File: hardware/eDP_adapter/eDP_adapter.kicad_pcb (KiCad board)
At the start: 2 copper layers, 36.3 x 28.4 mm, 89 parts, among them J1 DF12NB(3.0)-30DS-0.5V(51), J2 DF12NB(3.0)-30DS-0.5V(51), J3 Conn_01x40, J4 Barrel_Jack_MountingPin, Q1 2N7002WT1G, U1 NCS8801, U2 EA3036A, U3 MT3608

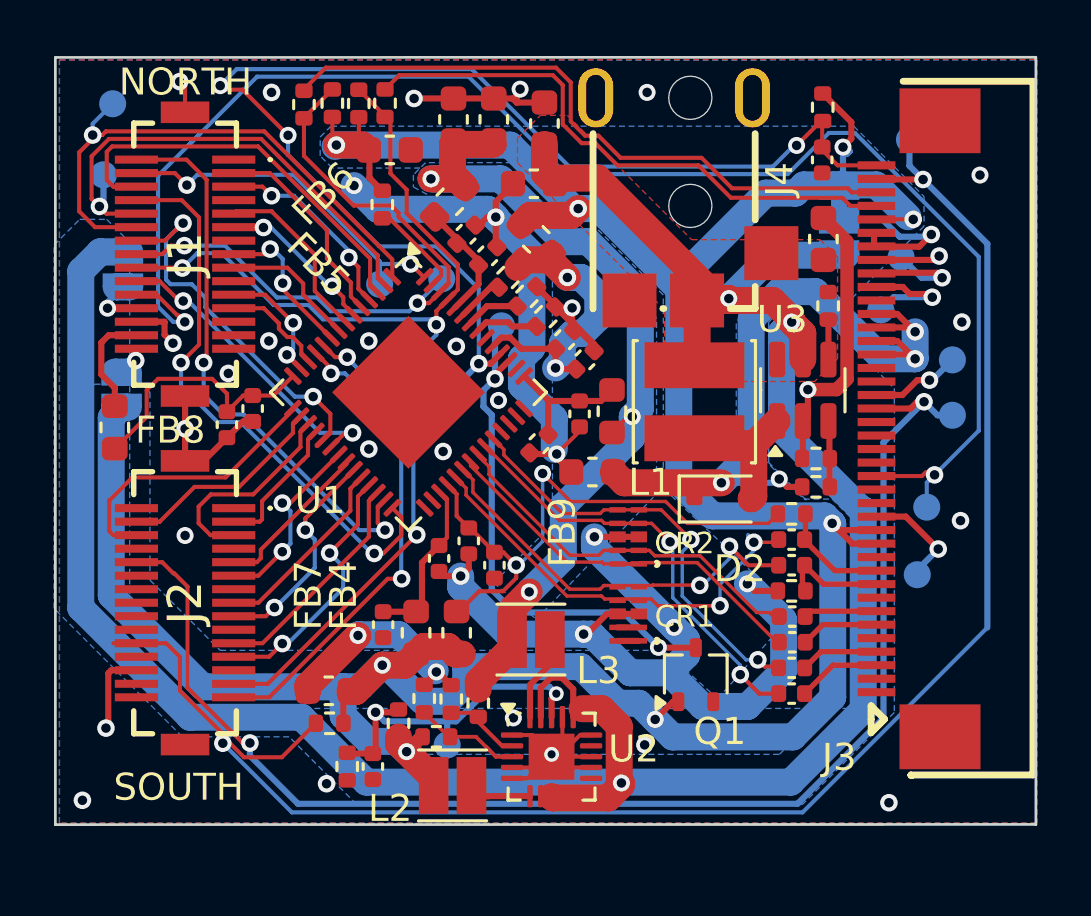
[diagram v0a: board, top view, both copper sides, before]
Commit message: make eDP adaoter 4 layer and misc fixes (like missing crystal)
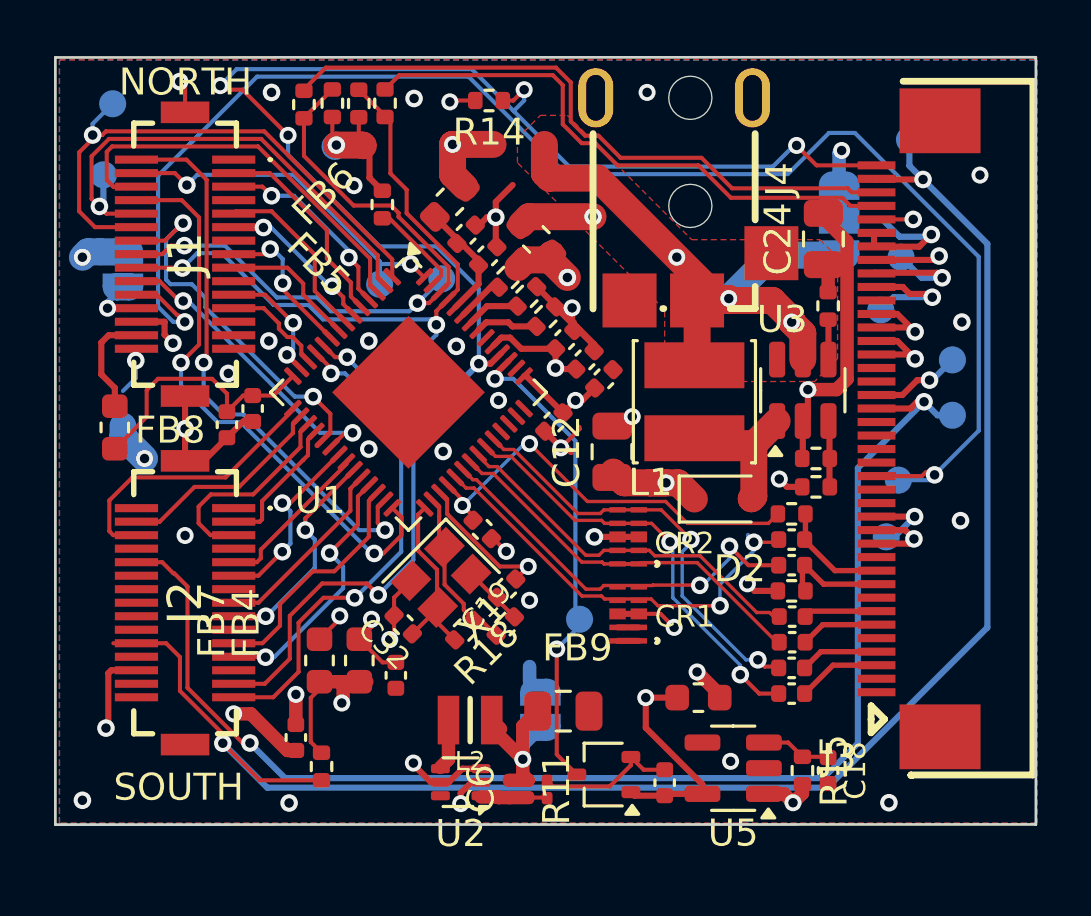
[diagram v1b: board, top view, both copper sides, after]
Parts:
- removed C28: 0.1uF, Capacitor_SMD:C_0402_1005Metric
- removed C29: 10u, Capacitor_SMD:C_0603_1608Metric
- removed C30: 0.1uF, Library:C_0402_1005Metric
- removed C31: 0.1u, Capacitor_SMD:C_0603_1608Metric
- removed L3: 1.5uH, Inductor_SMD:L_Cenker_CKCS201610
- removed R16, R17, R22: 100k, Resistor_SMD:R_0402_1005Metric
- removed TP10, TP11: TestPoint_Small, TestPoint:TestPoint_Pad_D1.0mm
- added C19: 18pF, Library:C_0402_1005Metric, F.Cu at (120.2, 133.9)
- added C32: 18pF, Library:C_0402_1005Metric, F.Cu at (116.5, 133.9)
- added R18: 1M, Resistor_SMD:R_0402_1005Metric, F.Cu at (118.7, 134.1)
- added TP8: TestPoint_Small, TestPoint:TestPoint_Pad_D1.0mm, B.Cu at (123.0, 133.7)
- added U5: TPNCP115ASN120T2G, Package_TO_SOT_SMD:SOT-23-5, F.Cu at (128.7, 139.2)
- added X1: 24MHz, CL=18PF, Library:Crystal_SMD_2520-4Pin_2.5x2.0mm, F.Cu at (117.9, 132.2)
- C12, C2: value 0.1u -> 10uF 25V; footprint Capacitor_SMD:C_0603_1608Metric -> Capacitor_SMD:C_0805_2012Metric
- C18: value 0.1u -> 0.1uF; footprint Capacitor_SMD:C_0603_1608Metric -> Library:C_0402_1005Metric
- C24: value 10u -> 10uF 25V; footprint Capacitor_SMD:C_0603_1608Metric -> Capacitor_SMD:C_0805_2012Metric
- C25: value 10u -> 2.2uF; footprint Capacitor_SMD:C_0603_1608Metric -> Library:C_0402_1005Metric
- C6: value 10u -> 100pF; footprint Capacitor_SMD:C_0603_1608Metric -> Capacitor_SMD:C_0201_0603Metric
- L2: value 1.5uH -> 2.2uH; footprint Inductor_SMD:L_Cenker_CKCS201610 -> Library:Murata_DFE201612P-2R2M=P2
- Q1: value 2N7002WT1G -> NX3008NBKW,115
- R11: value 150k 1% -> 15k; footprint Resistor_SMD:R_0402_1005Metric -> Resistor_SMD:R_0201_0603Metric
- R12: value 150k 1% -> 4.7k; footprint Resistor_SMD:R_0402_1005Metric -> Resistor_SMD:R_0201_0603Metric
- R14: value 680k 1% -> 100k
- R15: value 150k 1% -> 10k
- U2: value EA3036A -> TLV62569APDRL; footprint Package_DFN_QFN:WQFN-20-1EP_3x3mm_P0.4mm_EP1.7x1.7mm -> Package_TO_SOT_SMD:SOT-563
- moved C18 27.1 mm to (132.2, 139.3)
- moved R14 23.6 mm to (119.7, 114.5)
- moved C2 21.7 mm to (122.4, 137.1), turned to 0 degrees
- moved JP2 19.5 mm to (121.5, 137.1), turned to -90 degrees
- moved C12 13.6 mm to (124.2, 127.5), turned to 90 degrees
- moved R15 12.3 mm to (131.2, 139.3)
- moved C25 11.8 mm to (126.2, 139.8), turned to 90 degrees
- moved FB9 11.1 mm to (127.4, 136.6), turned to 0 degrees
- moved C6 7.60 mm to (120.4, 140.0), turned to 90 degrees
- moved C11 5.47 mm to (116.2, 135.8)
- moved C8 5.28 mm to (112.5, 138.1)
- moved R11 5.10 mm to (121.1, 140.0), turned to -90 degrees
- moved Q1 5.02 mm to (123.9, 139.4), turned to 180 degrees
- moved R12 4.88 mm to (121.8, 140.0)
- moved FB4 3.74 mm to (114.8, 135.2)
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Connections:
- C12 pad 1: GND -> /BACKLIGHT_POWER
- C12 pad 2: +1V2 -> GND
- C18 pad 1: GND -> Net-(U5-EN)
- C18 pad 2: +1V2 -> GND
- C2 pad 1: GND -> /+3V3_DISP
- C2 pad 2: +3V3 -> GND
- C24 pad 1: GND -> +5V
- C24 pad 2: +5V -> GND
- C25 pad 1: GND -> +1V2
- C25 pad 2: /BACKLIGHT_POWER -> GND
- C6 pad 1: GND -> Net-(U2-FB)
- C6 pad 2: +3V3 -> /+3V3_DISP
- J1 pad 30: +3V3_MCU -> +3V3
- J3 pad 12: +3V3 -> /+3V3_DISP
- J3 pad 13: +3V3 -> /+3V3_DISP
- JP2 pad 2: +3V3_MCU -> /+3V3_DISP
- L2 pad 1: +3V3 -> /+3V3_DISP
- L2 pad 2: Net-(U2-SW2) -> Net-(U2-SW)
- Q1 pad 1: +3V3 -> +1V2
- R11 pad 1: Net-(U2-FB2) -> /+3V3_DISP
- R11 pad 2: GND -> Net-(U2-FB)
- R12 pad 2: Net-(U2-FB3) -> Net-(U2-FB)
- R14 pad 1: Net-(U2-FB2) -> RSTB
- R15 pad 1: +1V2 -> Net-(U5-EN)
- R15 pad 2: Net-(U2-FB3) -> +3V3
- U1 pad 29: unconnected-(U1-XTALIN-Pad29) -> /XTALI
- U1 pad 30: unconnected-(U1-XTALOUT-Pad30) -> /XTALO
- U2 pad 1: GND -> Net-(U2-FB)
- U2 pad 2: Net-(U2-FB3) -> GND
- U2 pad 3: Net-(U2-FB2) -> +5V
- U2 pad 4: GND -> Net-(U2-SW)
- U2 pad 5: GND -> +5V
- U2 pad 6: Net-(U2-SW2) -> unconnected-(U2-NC-Pad6)
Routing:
- net GND: track 111.0 -> 56.9 mm, vias 38 -> 36
- net /+3V3_DISP: track 0.00 -> 28.7 mm, vias 0 -> 2
- net /BACKLIGHT_POWER: track 29.1 -> 11.9 mm
- net AVDD_1V2: track 5.48 -> 22.4 mm, vias 0 -> 2
- net XVDD_3V3: track 7.12 -> 20.2 mm, vias 0 -> 3
- net Net-(U2-EN3): track 12.7 -> 0.00 mm, vias 2 -> 0
- net /XTALI: track 0.00 -> 6.87 mm
- net /XTALO: track 0.00 -> 6.13 mm
- net +1V2: track 32.3 -> 36.7 mm
- net Net-(U2-FB2): track 4.11 -> 0.00 mm
- net AVDD_3V3: track 20.9 -> 24.2 mm, vias 2 -> 3
- net +3V3: track 116.6 -> 113.4 mm, vias 8 -> 9
- net Net-(U2-SW3): track 3.16 -> 0.00 mm
- net Net-(U2-FB3): track 2.87 -> 0.00 mm
- net Net-(U5-EN): track 0.00 -> 2.61 mm
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- added copper zone on In2.Cu, net +1V2
- added copper zone on In2.Cu, net +3V3
- added copper zone on In2.Cu, net +5V
- added copper zone on In1.Cu, net /BACKLIGHT_POWER
- added copper zone on In2.Cu, net AVDD_3V3
- added copper zone on In2.Cu, net DVDD_3V3
- added copper zone on In1.Cu, net GND
- removed copper zone on B.Cu, net +1V2
- removed copper zone on B.Cu, net +3V3
- removed copper zone on B.Cu, net +5V
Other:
- copper layers 2 -> 4

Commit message: fixed mixup of pins G5/G4 (3rd diff pair ODD) and DE/PCLK (3rd diff pair EVEN), now with correct polarity for diff pairs
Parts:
- added C26: 0.1uF, Library:C_0402_1005Metric, F.Cu at (132.3, 115.0)
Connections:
- J2 pad 4: G4 -> G5
- J2 pad 6: G5 -> G4
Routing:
- net G5: track 10.4 -> 7.99 mm
- net RSTB: track 47.1 -> 48.5 mm
- net G4: track 7.89 -> 8.42 mm

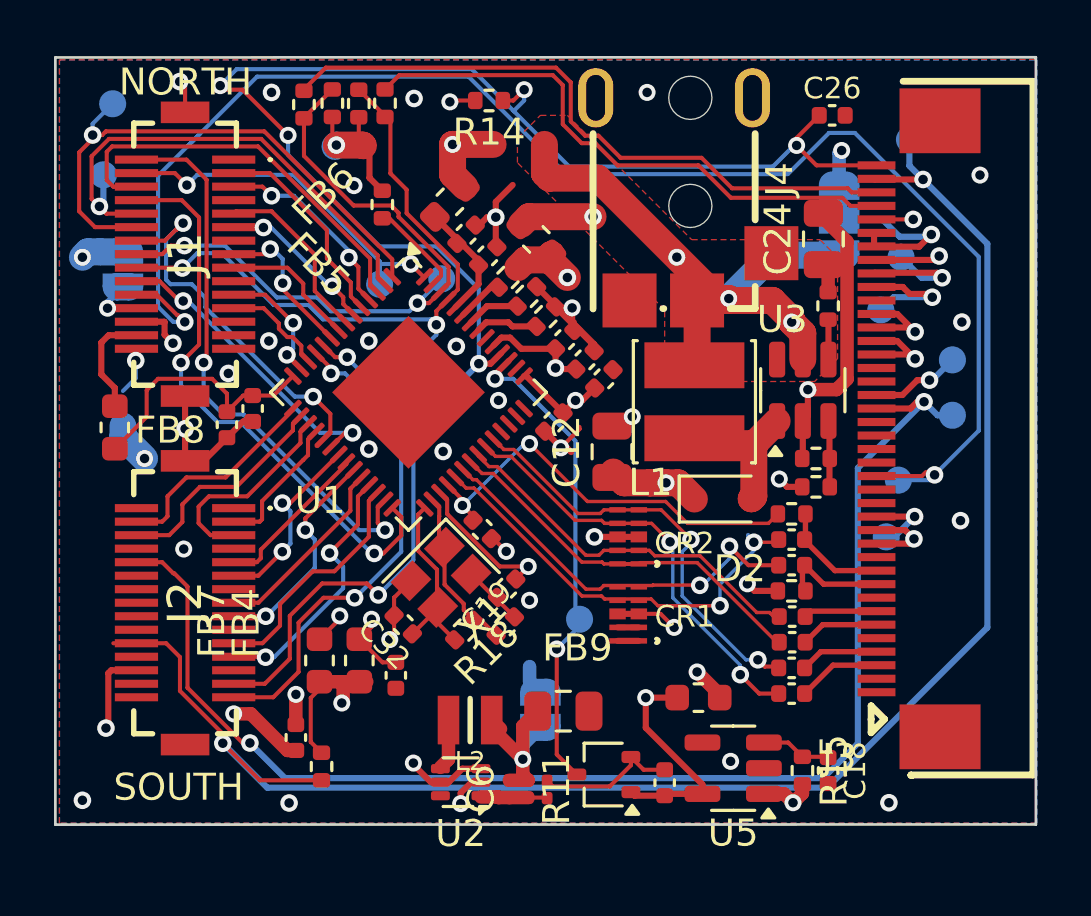
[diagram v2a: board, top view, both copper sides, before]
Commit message: Add I2C connector for touch and replace 40pin touch with 30pin. Separate schematics in sheets. Impedance control on diff pairs
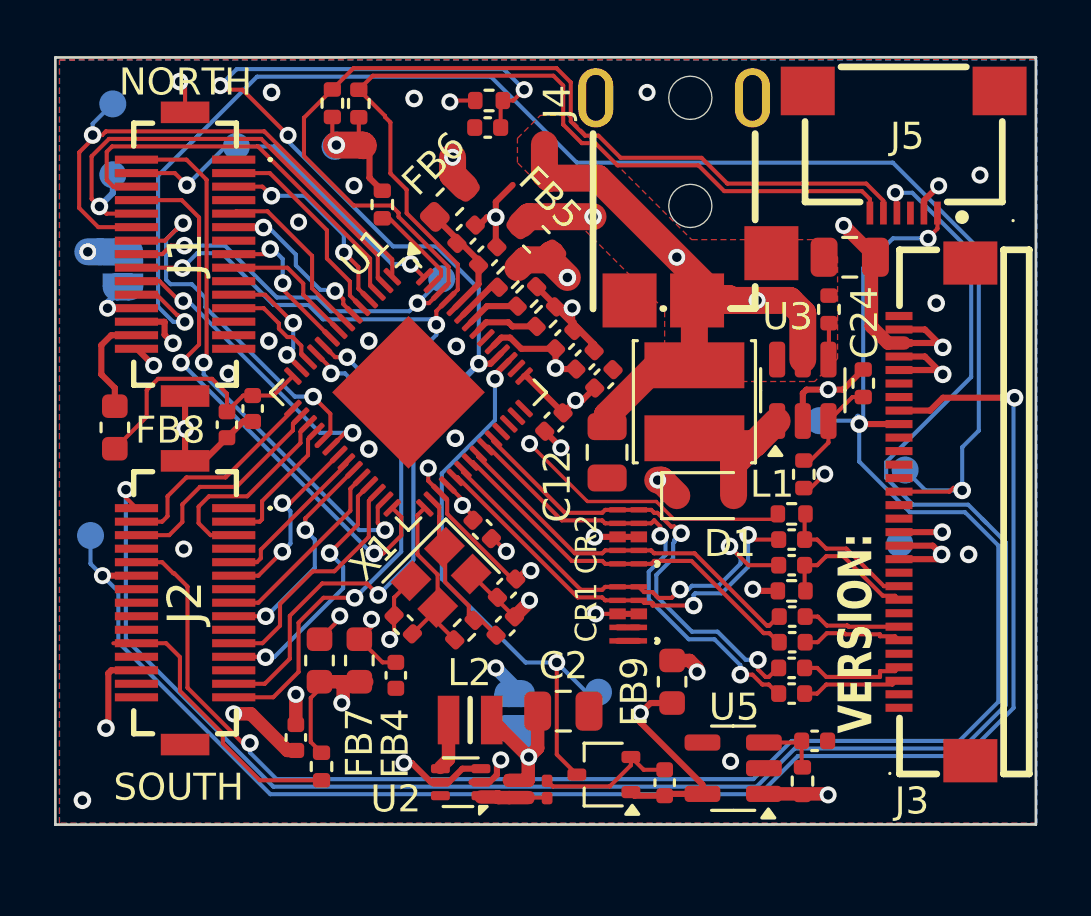
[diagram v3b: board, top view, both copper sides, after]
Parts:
- removed D2: 1N5819WS, Diode_SMD:D_SOD-323
- removed JP3: SolderJumper_3_Bridged12, Jumper:SolderJumper-3_P1.3mm_Bridged12_RoundedPad1.0x1.5mm
- removed R10, R13: 0, Resistor_SMD:R_0402_1005Metric
- removed R20: 150K 1%, Resistor_SMD:R_0402_1005Metric
- removed R21: 8.06K 1%, Resistor_SMD:R_0402_1005Metric
- removed TP1, TP15, TP16, TP2, TP3: TestPoint_Small, TestPoint:TestPoint_Pad_D1.0mm
- added D1: 1N5819WS, Diode_SMD:D_SOD-323, F.Cu at (127.7, 129.1)
- added J5: Conn_01x06_Socket, easyeda2kicad:FPC-SMD_FH52K-6S-0.5SH, F.Cu at (135.0, 116.4)
- added R16: 10k, Resistor_SMD:R_0402_1005Metric, F.Cu at (132.2, 122.2)
- added R17: 8.06K 1%, Resistor_SMD:R_0402_1005Metric, F.Cu at (133.5, 125.0)
- added TP10: TestPoint_Small, TestPoint:TestPoint_Pad_D1.0mm, B.Cu at (110.3, 116.2)
- added TP11: TestPoint_Small, TestPoint:TestPoint_Pad_D1.0mm, B.Cu at (105.7, 117.2)
- J3: value Conn_01x40 -> Conn_01x30; footprint Library:FPC-SMD_40P-P0.50_L4.4-W25.6 -> easyeda2kicad:FPC-SMD_30P-P0.50_FPC-0.5FX-30PWBH15
- R19: value 10k -> 150K 1%
- moved G*** 33.3 mm to (136.4, 114.6)
- moved TP4 32.6 mm to (104.9, 130.6)
- moved TP12 13.8 mm to (105.7, 114.6)
- moved TP14 13.4 mm to (117.1, 123.8)
- moved C26 12.8 mm to (119.6, 115.5), turned to 180 degrees
- moved R19 6.30 mm to (131.3, 128.3), turned to -90 degrees
- moved TP5 4.93 mm to (131.9, 126.3)
- moved G*** 4.25 mm to (127.3, 132.5)
- moved J3 3.23 mm to (136.1, 129.7)
- moved TP8 2.79 mm to (123.7, 136.4)
- moved TP13 2.76 mm to (117.9, 121.1)
- moved C18 1.21 mm to (131.7, 138.2), turned to 0 degrees
- moved C24 1.19 mm to (133.0, 120.3), turned to 180 degrees
- moved FB9 1.14 mm to (126.4, 136.0), turned to 90 degrees
- moved JP2 0.95 mm to (120.6, 137.1)
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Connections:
- net +5V_MCU renamed Net-(J1-23)
- net /+3V3_DISP renamed +3V3_DISP
- net /AUX0_N renamed AUX0_N
- net /AUX0_P renamed AUX0_P
- net /LCD_TEST renamed /IO/LCD_TEST
- net /SCK2 renamed /IO/SCK2
- net /SDA2 renamed /IO/SDA2
- net /TX0_N renamed TX0_N
- net /TX0_P renamed TX0_P
- net /TX1_N renamed TX1_N
- net /TX1_P renamed TX1_P
- net Net-(U1-DPAUX_N) renamed /DPAUX_N
- net Net-(U1-DPAUX_P) renamed /DPAUX_P
- net Net-(U1-DPO0_N) renamed /DPO0_N
- net Net-(U1-DPO0_P) renamed /DPO0_P
- net Net-(U1-DPO1_N) renamed /DPO1_N
- net Net-(U1-DPO1_P) renamed /DPO1_P
- C12 pad 1: /BACKLIGHT_POWER -> +5V
- C24 pad 1: +5V -> BACKLIGHT_POWER
- C32 pad 1: /XTALI -> GND
- C32 pad 2: GND -> /XTALI
- J2 pad 12: /TP_PWM -> /IO/LCD_PWM
- J2 pad 2: unconnected-(J2-1-Pad2) -> /IO/TP_INT
- J3 pad 23: /LCD_PWM -> /IO/LCD_PWM
- J3 pad 26: /BACKLIGHT_POWER -> BACKLIGHT_POWER
- J3 pad 27: /BACKLIGHT_POWER -> BACKLIGHT_POWER
- J3 pad 28: /BACKLIGHT_POWER -> BACKLIGHT_POWER
- J3 pad 29: /BACKLIGHT_POWER -> BACKLIGHT_POWER
- J3 pad 31: /TP_D- -> (no net)
- J3 pad 32: /TP_D+ -> (no net)
- R19 pad 1: Net-(U3-EN) -> Net-(U3-FB)
- R19 pad 2: +5V -> BACKLIGHT_POWER
- TP12 pad 1: SDA -> LCD_VSYNC
- TP13 pad 1: SCK -> SDA
- TP14 pad 1: LCD_HSYNC -> SCK
- TP4 pad 1: /LCD_PWM -> /IO/LCD_PWM
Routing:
- net /IO/TP_INT: track 0.00 -> 68.3 mm, vias 0 -> 2
- net /IO/LCD_PWM: track 0.00 -> 58.3 mm, vias 0 -> 2
- net HPD2: track 63.3 -> 10.7 mm, vias 2 -> 0
- net BACKLIGHT_POWER: track 0.00 -> 34.3 mm, vias 0 -> 5
- net +3V3: track 113.4 -> 84.4 mm, vias 9 -> 8
- net /TP_SDA: track 24.5 -> 0.00 mm
- net SDA: track 25.1 -> 49.1 mm
- net SCK: track 24.2 -> 46.6 mm
- net /TP_SCK: track 21.5 -> 0.00 mm
- net RSTB: track 48.5 -> 32.0 mm, vias 5 -> 4
- net PSEL: track 49.6 -> 65.7 mm, vias 2 -> 3
- net /BACKLIGHT_POWER: track 11.9 -> 0.00 mm, vias 4 -> 0
- net GND: track 56.9 -> 47.2 mm, vias 36 -> 33
- net XVDD_3V3: track 20.2 -> 28.2 mm, vias 3 -> 4
- net AVDD_3V3: track 24.2 -> 31.7 mm
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- added copper zone on In1.Cu, net BACKLIGHT_POWER
- removed copper zone on In1.Cu, net /BACKLIGHT_POWER
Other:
- board text added: "JLC04161H-3313A differential non-coplanar 100ohm: 0.127mm space, 0.1537mm"
- board text added: "VERSION:"
- board text added: "eDP Adapter V0.10"
- board text removed: "eDP Adapter V0.09"
